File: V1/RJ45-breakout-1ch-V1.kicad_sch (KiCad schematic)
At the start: 2 parts, among them J1 RJ45, J2 SWITCHES

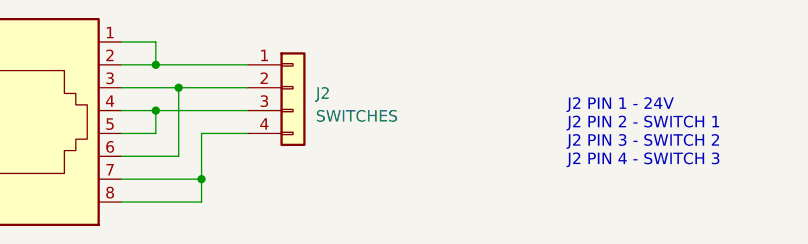
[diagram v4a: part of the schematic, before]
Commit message: Cosmetic enhancements to PCB
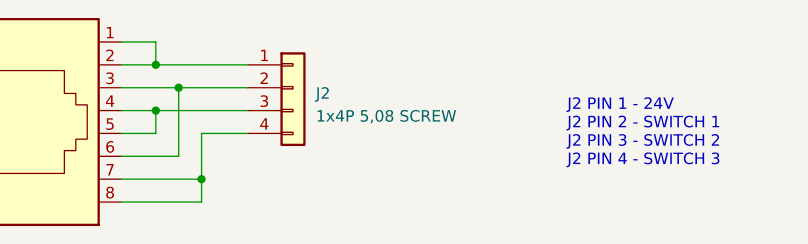
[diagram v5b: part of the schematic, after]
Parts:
- J2: value SWITCHES -> 1x4P 5,08 SCREW
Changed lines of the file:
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@@
       (effects (font (size 1.27 1.27)) (justify left))
     )
-    (property "Value" "SWITCHES" (at 165.1 102.235 0)
+    (property "Value" "1x4P 5,08 SCREW" (at 165.1 102.235 0)
       (effects (font (size 1.27 1.27)) (justify left))
     )
